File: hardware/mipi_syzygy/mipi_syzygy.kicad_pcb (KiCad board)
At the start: 4 copper layers, 45 x 12 mm, 3 parts, among them J2 SYZYGY_STD

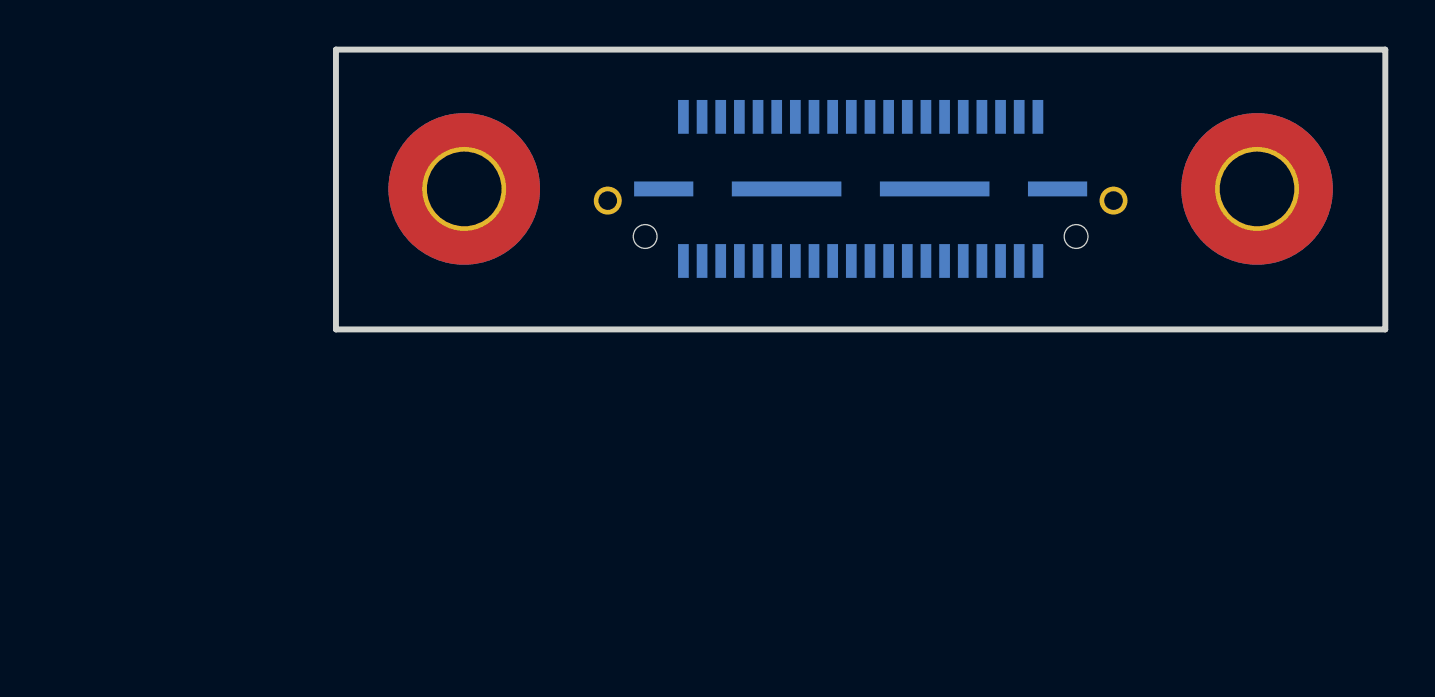
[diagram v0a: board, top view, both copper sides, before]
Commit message: Routed mipi board
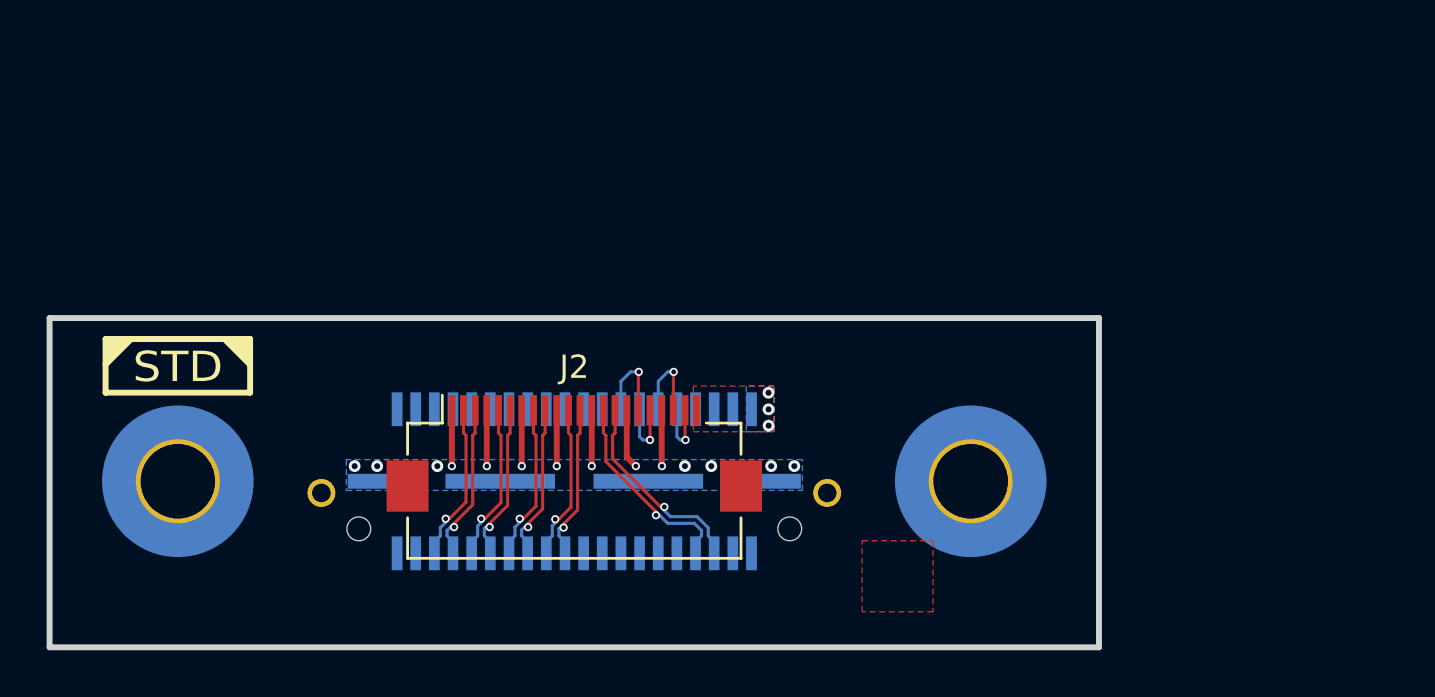
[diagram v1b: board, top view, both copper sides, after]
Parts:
- removed H1, H2: MountingHole_Pad, SYZYGY:MountingHole_3.2mm_M3_6.5mm_Pad_TopBottom
- added ? (x2): , , F.Cu at (167.2, 96.5)
- added ? (x2): , , F.Cu at (133.2, 96.5)
- added G***: LOGO, LOGO, F.Cu at (164.1, 100.6)
- added J1: SYZYGY_STD, SYZYGY:QTE-020-01-F-D-A, B.Cu at (150.2, 96.5)
- added REF**: SYZYGY_STD_Logo, SYZYGY:SYZYGY_STD_Logo, F.Cu at (136.3, 92.7)
- J2: value SYZYGY_STD -> Conn_01x22; footprint SYZYGY:QTE-020-01-F-D-A -> Connector_FFC-FPC:Hirose_FH12-22S-0.5SH_1x22-1MP_P0.50mm_Horizontal; moved to F.Cu
- moved J2 16.7 mm to (150.2, 95.3)
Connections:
- J2 pad 1: unconnected-(J2-Pad1) -> GND
- J2 pad 10: /CAM_D1_P -> GND
- J2 pad 11: unconnected-(J2-Pad11) -> /CAM_D3_P
- J2 pad 12: /CAM_D1_N -> /CAM_D3_N
- J2 pad 13: unconnected-(J2-Pad13) -> GND
- J2 pad 14: unconnected-(J2-Pad14) -> /CAM_CK_P
- J2 pad 15: unconnected-(J2-Pad15) -> /CAM_CK_N
- J2 pad 16: unconnected-(J2-Pad16) -> GND
- J2 pad 17: unconnected-(J2-Pad17) -> /CAM_IO0
- J2 pad 18: unconnected-(J2-Pad18) -> /CAM_IO1
- J2 pad 19: unconnected-(J2-Pad19) -> GND
- J2 pad 2: unconnected-(J2-Pad2) -> /CAM_D0_P
- J2 pad 20: unconnected-(J2-Pad20) -> /CAM_SCL
- J2 pad 21: /CAM_IO0 -> /CAM_SDA
- J2 pad 22: unconnected-(J2-Pad22) -> +3.3V
- J2 pad 3: unconnected-(J2-Pad3) -> /CAM_D0_N
- J2 pad 4: unconnected-(J2-Pad4) -> GND
- J2 pad 5: unconnected-(J2-Pad5) -> /CAM_D1_P
- J2 pad 6: /CAM_D0_P -> /CAM_D1_N
- J2 pad 7: unconnected-(J2-Pad7) -> GND
- J2 pad 8: /CAM_D0_N -> /CAM_D2_P
- J2 pad 9: unconnected-(J2-Pad9) -> /CAM_D2_N
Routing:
- net GND: track 0.00 -> 16.8 mm, vias 0 -> 14
- net /CAM_CK_P: track 0.00 -> 8.75 mm, vias 0 -> 1
- net /CAM_CK_N: track 0.00 -> 8.75 mm, vias 0 -> 1
- net /CAM_D0_P: track 0.00 -> 6.83 mm, vias 0 -> 1
- net /CAM_D0_N: track 0.00 -> 6.83 mm, vias 0 -> 1
- net /CAM_D1_N: track 0.00 -> 6.79 mm, vias 0 -> 1
- net /CAM_D1_P: track 0.00 -> 6.79 mm, vias 0 -> 1
- net /CAM_D2_P: track 0.00 -> 6.75 mm, vias 0 -> 1
- net /CAM_D2_N: track 0.00 -> 6.75 mm, vias 0 -> 1
- net /CAM_D3_P: track 0.00 -> 6.71 mm, vias 0 -> 1
- net /CAM_D3_N: track 0.00 -> 6.71 mm, vias 0 -> 1
- net /CAM_IO0: track 0.00 -> 3.86 mm, vias 0 -> 1
- net /CAM_SCL: track 0.00 -> 3.67 mm, vias 0 -> 1
- net /CAM_IO1: track 0.00 -> 2.96 mm, vias 0 -> 1
- net /CAM_SDA: track 0.00 -> 2.89 mm, vias 0 -> 1
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- added copper zone on F.Cu, net (none)
- added copper zone on B.Cu, net +3.3V
- added copper zone on F.Cu, net +3.3V
- added copper zone on B.Cu, net GND
- added copper zone on In1.Cu, net GND
- added copper zone on In2.Cu, net GND
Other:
- board size 45 x 12 mm -> 45 x 14.1 mm
